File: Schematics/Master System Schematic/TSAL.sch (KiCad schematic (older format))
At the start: 0 parts

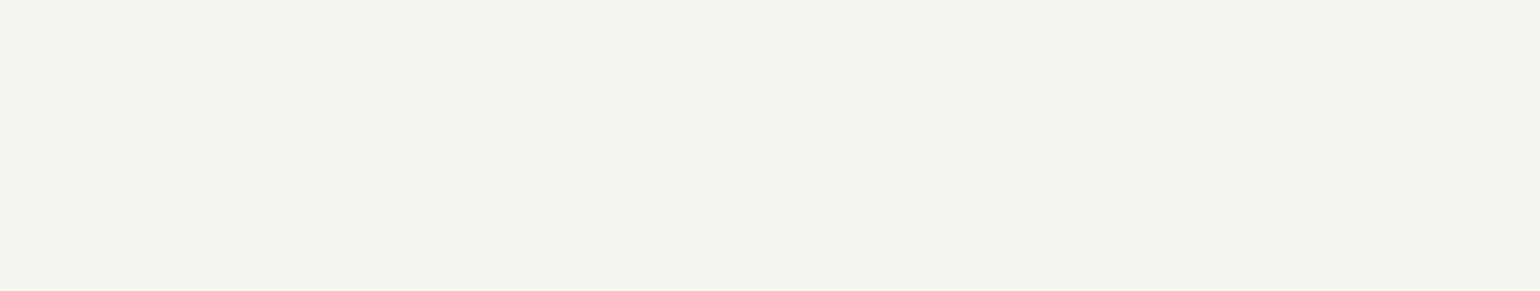
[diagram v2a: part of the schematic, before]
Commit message: TSAL call out
Redirect to altium for TSAL
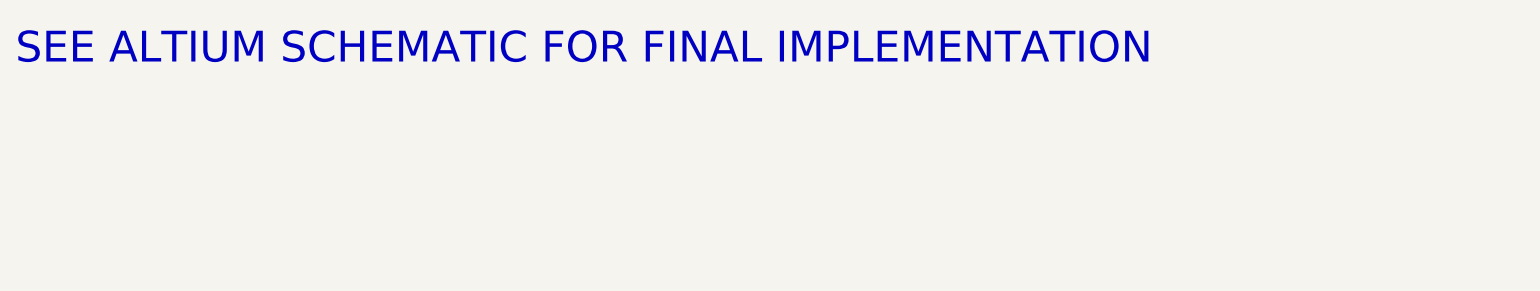
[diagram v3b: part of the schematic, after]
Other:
- note added: "SEE ALTIUM SCHEMATIC FOR FINAL IMPLEMENTATION"
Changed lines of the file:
@@
 $Descr A4 11693 8268
 encoding utf-8
-Sheet 9 24
+Sheet 23 24
 Title ""
 Date ""
@@
 Text HLabel 10250 3400 0    50   Input ~ 0
 TSAL_LED-
+Text Notes 2650 1300 0    157  ~ 0
+SEE ALTIUM SCHEMATIC FOR FINAL IMPLEMENTATION
 $EndSCHEMATC
